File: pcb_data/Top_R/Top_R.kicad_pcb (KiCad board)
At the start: 2 copper layers, 186.9 x 96.4 mm, 93 parts, among them U1 XIAO-nRF52840

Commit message: remove zone
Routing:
- removed copper zone on B.Cu, net GND
- removed copper zone on F.Cu, net GND
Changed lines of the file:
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@@
 		(net 55)
-	)
-	(zone
-		(net 52)
-		(net_name "GND")
-		(layers "F.Cu" "B.Cu")
-		(hatch edge 0.5)
-		(connect_pads
-			(clearance 0.5)
-		)
-		(min_thickness 0.25)
-		(filled_areas_thickness no)
-		(fill yes
-			(thermal_gap 0.5)
-			(thermal_bridge_width 0.5)
-		)
-		(polygon
-			(pts
-				(xy 251.817399 48.815666) (xy 250.626773 47.62504) (xy 77.39069 47.62504) (xy 75.604751 48.815666)
-				(xy 75.604751 68.460995) (xy 67.270369 68.460995) (xy 66.079743 69.651621) (xy 66.079743 82.748507)
-				(xy 67.270369 83.939133) (xy 70.842247 83.939133) (xy 70.842247 101.798523) (xy 72.032873 102.989149)
-				(xy 75.604751 102.989149) (xy 75.604751 125.611043) (xy 67.270369 125.611043) (xy 66.079743 126.801669)
-				(xy 66.079743 141.684494) (xy 67.270369 142.87512) (xy 250.626773 142.87512) (xy 251.817399 141.684494)
-			)
-		)
 	)
 	(embedded_fonts no)

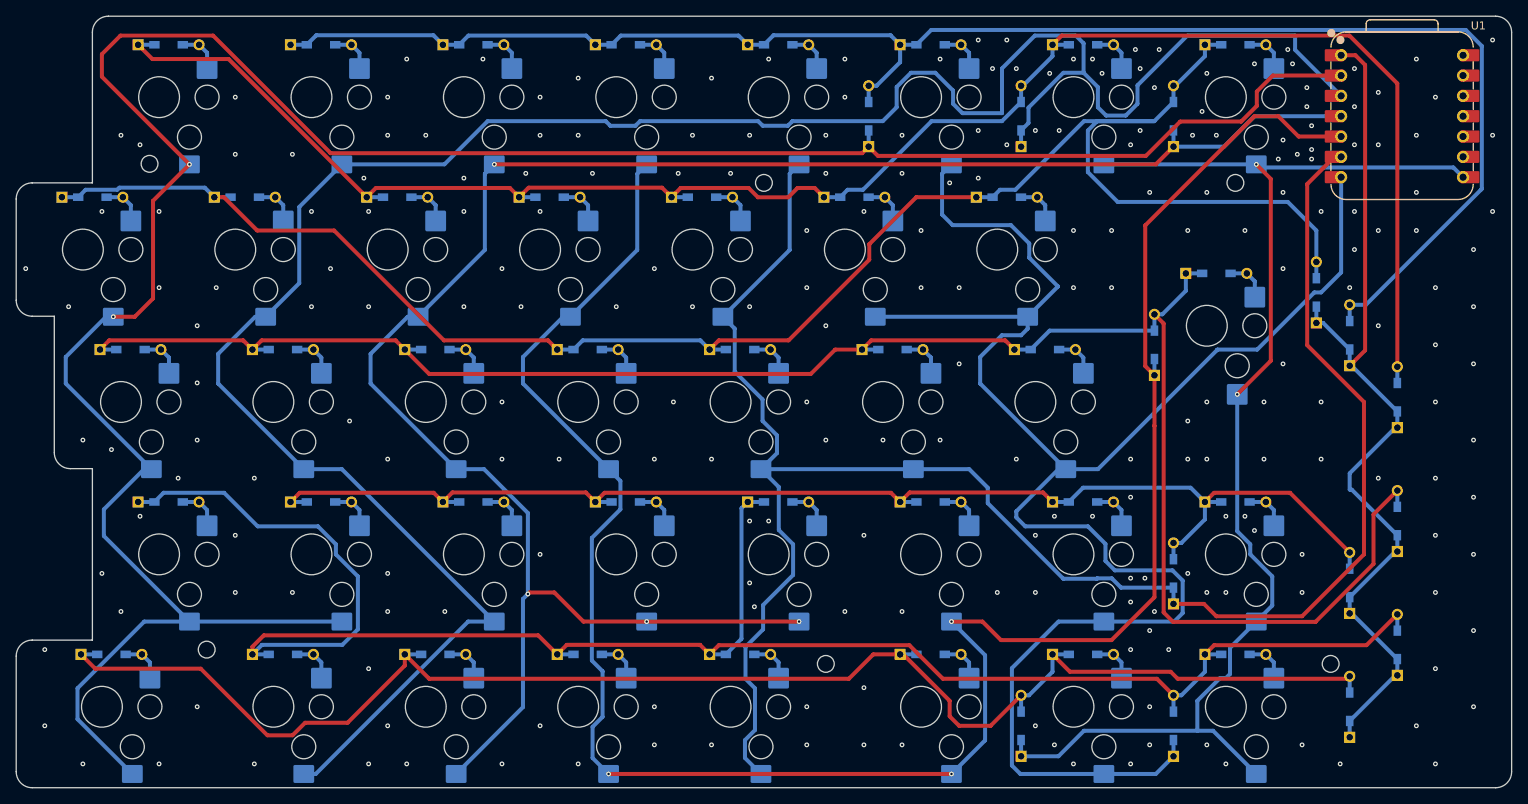
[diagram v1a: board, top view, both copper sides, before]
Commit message: remove segment
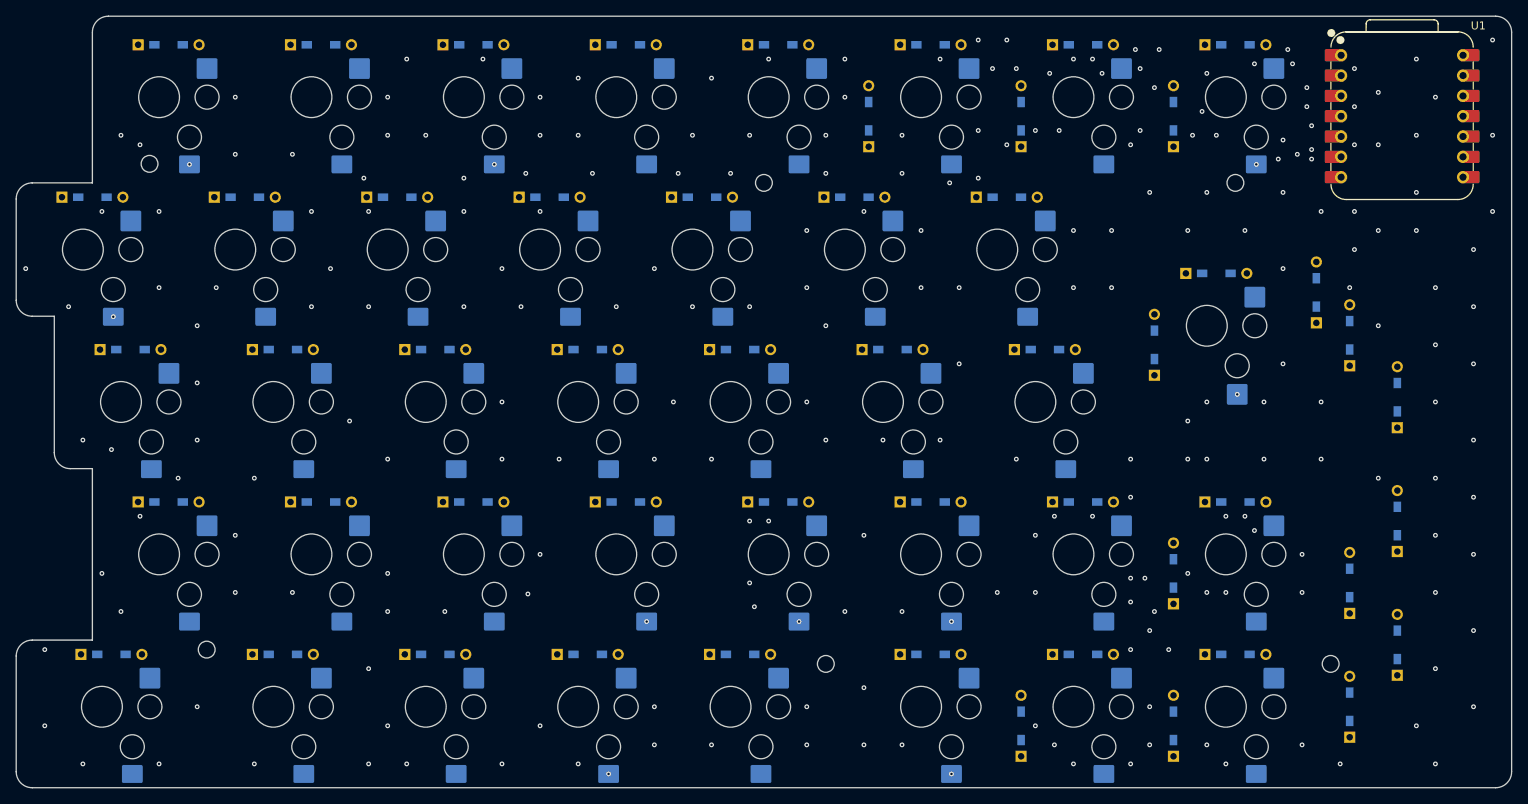
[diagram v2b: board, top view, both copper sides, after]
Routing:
- net IO 7: track 315.0 -> 0.00 mm
- net IO 8: track 286.9 -> 0.00 mm
- net IO 10: track 264.8 -> 0.00 mm
- net Net-(D0-12-K): track 243.7 -> 0.00 mm
- net IO 9: track 243.1 -> 0.00 mm
- net Net-(D0-10-K): track 237.6 -> 0.00 mm
- net IO 12: track 232.8 -> 0.00 mm
- net IO 11: track 232.4 -> 0.00 mm
- net Net-(D0-8-K): track 230.0 -> 0.00 mm
- net Net-(D0-9-K): track 229.3 -> 0.00 mm
- net Net-(D1-7-K): track 206.2 -> 0.00 mm
- net Net-(D0-13-K): track 193.7 -> 0.00 mm
- net Net-(D0-11-K): track 162.9 -> 0.00 mm
- net IO 13: track 160.0 -> 0.00 mm
- net INTR_R: track 113.6 -> 0.00 mm
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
